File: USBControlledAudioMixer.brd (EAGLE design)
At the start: 42.5 x 40 mm, 50 parts, among them IC1 TDA7448, IC2 TS912, IC3 MEGA8-AI, J2 AVR_SPI_PRG_6NS, Q1 16MHz, U1 LMR62014

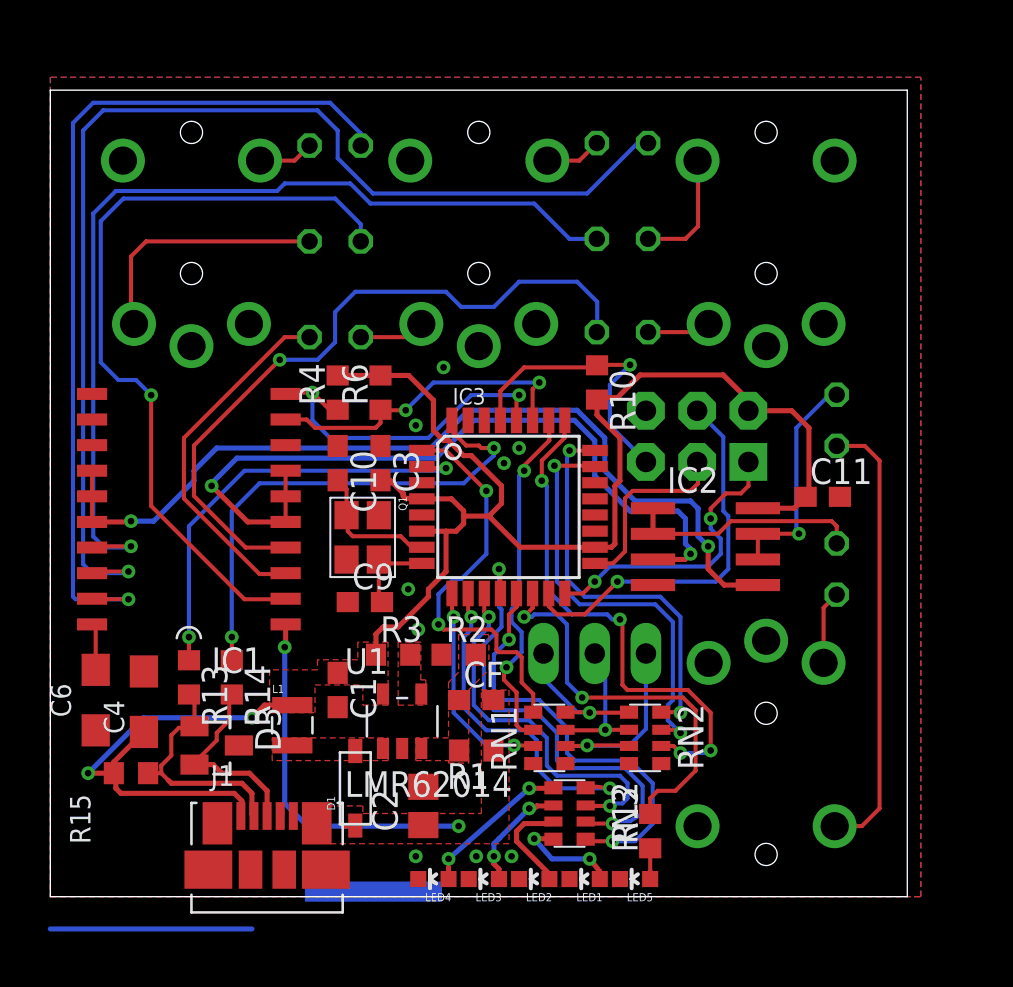
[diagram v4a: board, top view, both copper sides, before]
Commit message: Refactored whole board because due to case layout constraint, the regular through-hole film capacitors couldn't be used anymore. We're now using 1206 SMD film capacitors.
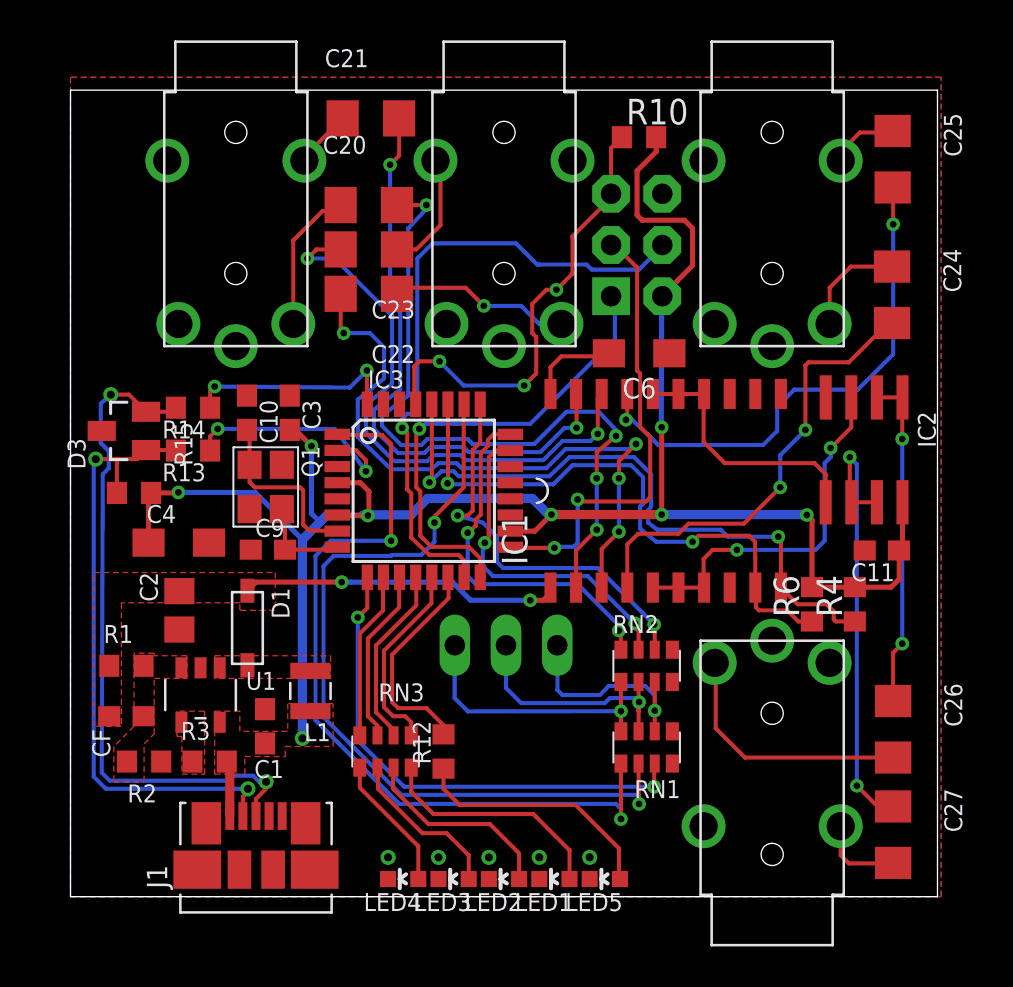
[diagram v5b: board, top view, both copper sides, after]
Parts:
- C20, C21, C22, C23, C24, C25, C26, C27: device rcl:C025-050X050 -> rcl:C1206
- JP2: device pinhead:1X03/90 -> TinyMix3:1X03/90_MOLEX_4094
- moved C6 32.0 mm to (29.2, 26.9), turned to 0 degrees
- moved R4 27.7 mm to (39.9, 14.5)
- moved R6 23.8 mm to (37.8, 14.5)
- moved IC1 23.7 mm to (30.5, 20.1), turned to 0 degrees
- moved C27 20.7 mm to (41.8, 3.08), flipped to the top
- moved R1 17.9 mm to (3.77, 11.4), turned to 0 degrees
- moved CF 17.4 mm to (3.77, 8.95), turned to 180 degrees
- moved R2 16.5 mm to (4.65, 6.70), turned to 180 degrees
- moved D3 16.3 mm to (3.65, 23.1), turned to 90 degrees
- moved C2 15.5 mm to (6.40, 14.2), turned to 270 degrees
- moved C25 14.0 mm to (41.8, 36.6), flipped to the top, turned to 270 degrees
- moved R15 13.9 mm to (4.15, 20.0), turned to 180 degrees
- moved C23 13.6 mm to (15.8, 32.1), flipped to the top
- moved R14 13.5 mm to (7.08, 24.2), turned to 180 degrees
- moved C24 13.5 mm to (41.8, 29.9), flipped to the top, turned to 270 degrees
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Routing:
- net OUT_R: track 44.2 -> 13.0 mm, vias 2 -> 0
- net IN_2_R: track 57.8 -> 28.5 mm, vias 1 -> 2
- net N$13: track 9.63 -> 33.4 mm, vias 0 -> 2
- net TOUCH_SEND_+: track 17.7 -> 40.9 mm
- net IN_3_R: track 46.8 -> 25.9 mm, vias 1 -> 2
- net OUT_L: track 38.7 -> 18.0 mm
- net TOUCH_SEND_-: track 20.1 -> 40.1 mm
- net N$11: track 11.8 -> 31.0 mm, vias 0 -> 2
- net N$26: track 22.3 -> 4.22 mm
- net SCL: track 17.2 -> 32.3 mm
- net IN_1_R: track 44.0 -> 29.4 mm, vias 1 -> 2
- net TOUCH_SEND_CHAN: track 10.6 -> 25.1 mm
- net IN_2_L: track 17.9 -> 32.4 mm, vias 0 -> 4
- net D+: track 24.8 -> 10.7 mm
- net LED2: track 23.0 -> 9.04 mm, vias 2 -> 0
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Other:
- board size 42.5 x 40 mm -> 43 x 40 mm

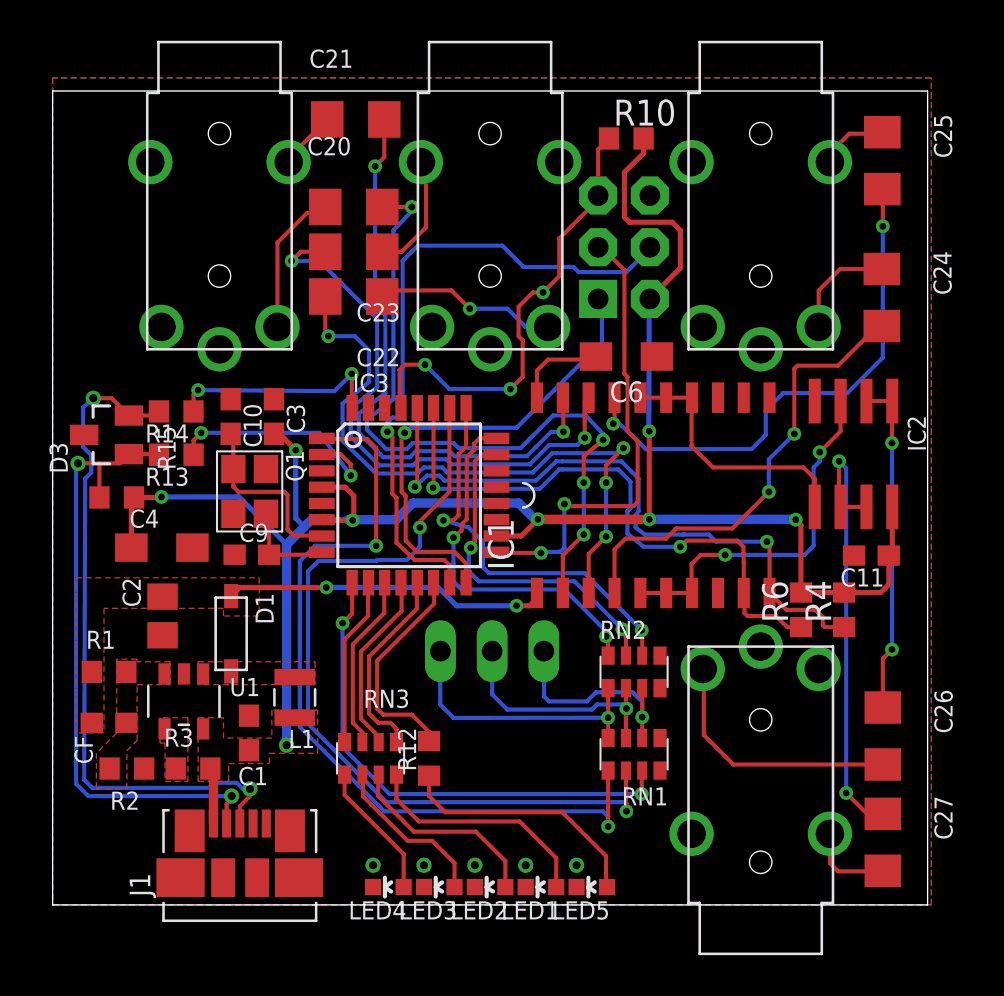
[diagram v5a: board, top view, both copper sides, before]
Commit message: Semi-finalized board, front and back panel Added 100nF capacitor for the TDA7448 mixer
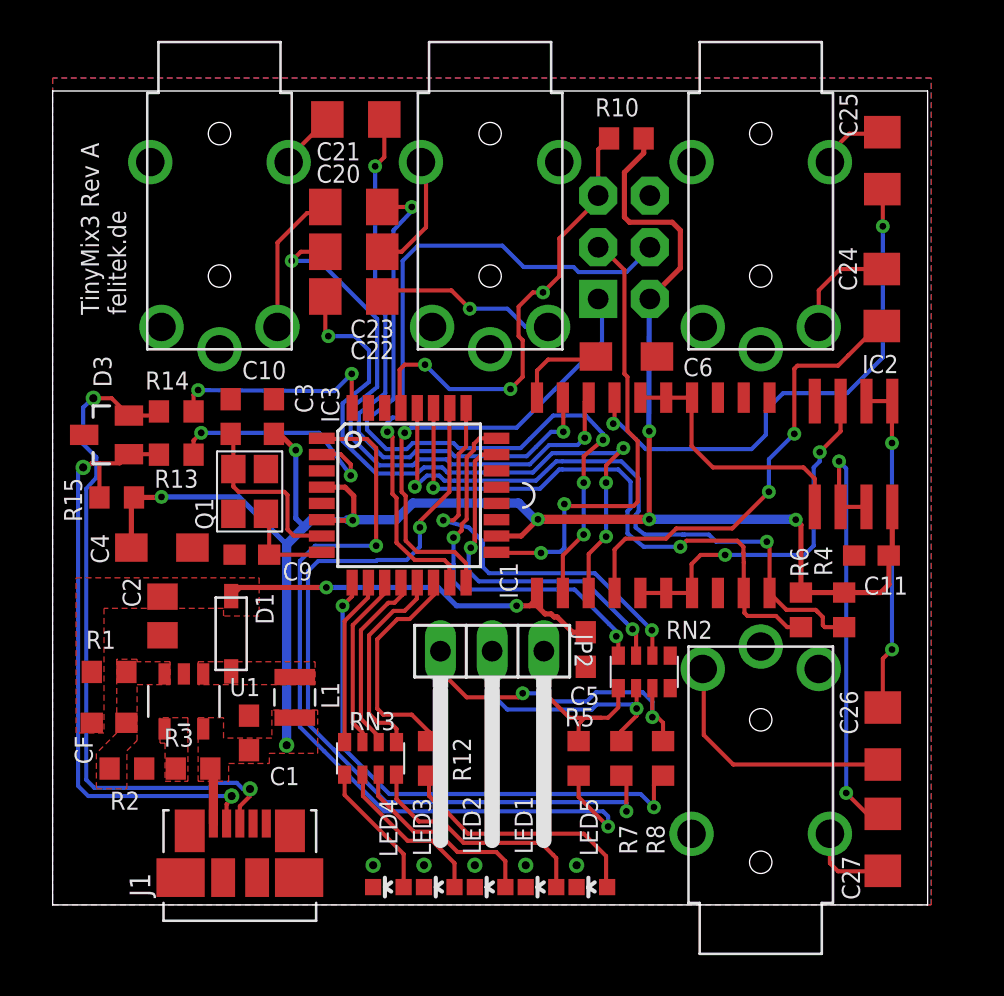
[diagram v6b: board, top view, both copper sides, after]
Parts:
- removed RN1: 1M, Simplex-rlc:YC164
- added C5: 100n, rcl:C0603
- added R5, R7, R8: 22M, rcl:R0603
- moved RN2 0.50 mm to (30.1, 11.4)
- flipped JP2 to the top
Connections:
- net +9V: now also C5.1
- net GND: now also C5.2
- net N$18: now also R5.2; no longer RN1.4
- net N$19: now also R7.2; no longer RN1.3
- net N$20: now also R8.2; no longer RN1.2
- net TOUCH_SEND_+: now also R7.1; no longer RN1.6
- net TOUCH_SEND_-: now also R5.1; no longer RN1.5
- net TOUCH_SEND_CHAN: now also R8.1; no longer RN1.7
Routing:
- net N$20: track 10.7 -> 16.3 mm, vias 1 -> 2
- net N$18: track 13.6 -> 9.43 mm, vias 1 -> 0
- net +9V: track 16.0 -> 19.2 mm
- net TOUCH_SEND_CHAN: track 25.1 -> 26.5 mm
- net TOUCH_RCV_+: track 17.4 -> 18.0 mm
- net TOUCH_RCV_CHAN: track 20.2 -> 20.7 mm
- net TOUCH_RCV_-: track 18.2 -> 18.7 mm
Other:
- board text added: "TinyMix3 Rev A felitek.de"

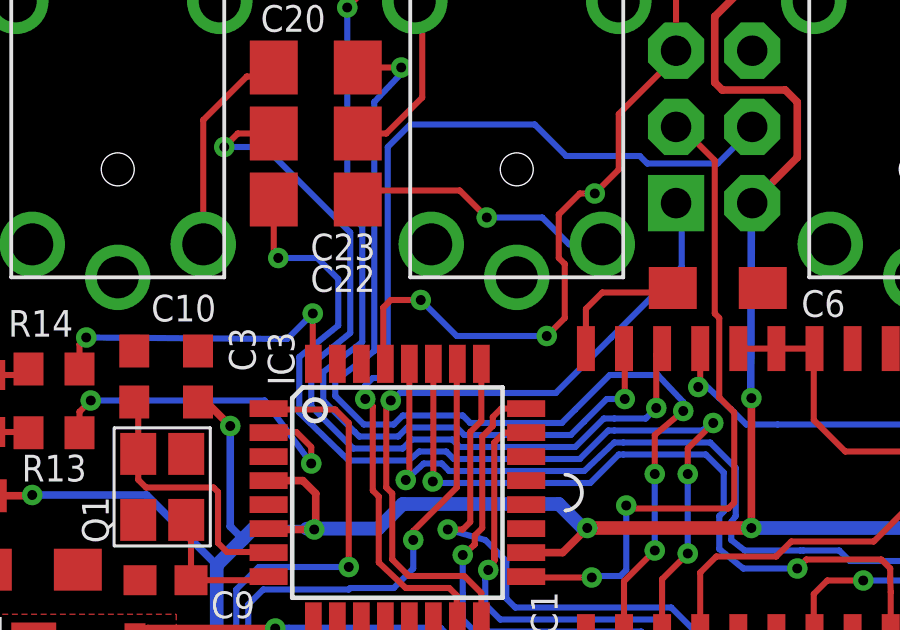
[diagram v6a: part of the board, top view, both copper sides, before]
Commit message: Added ESD protection for the RESET line
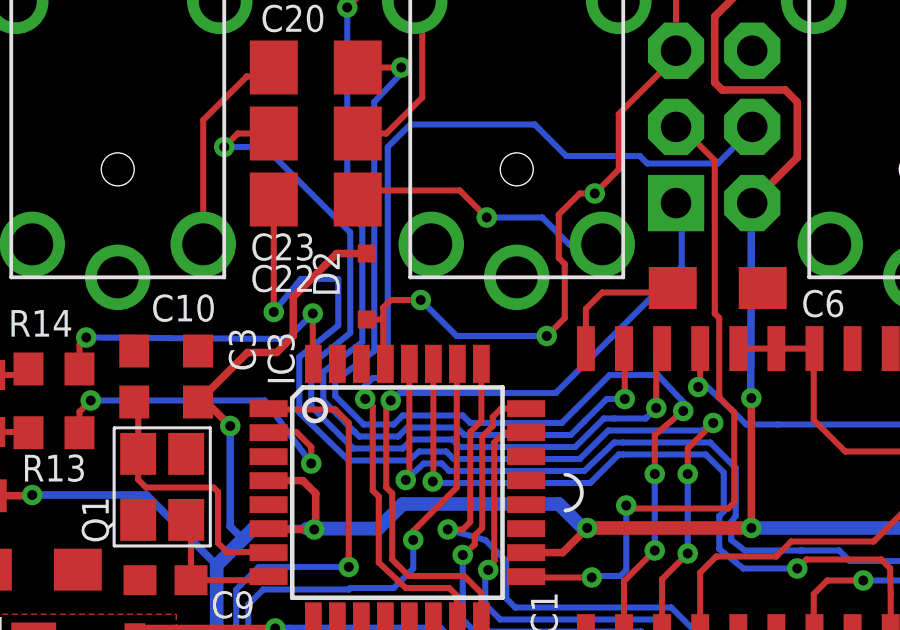
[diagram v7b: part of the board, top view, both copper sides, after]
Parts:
- added D2: (no value), diode:SOD323-R
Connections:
- net +5V: now also D2.C
- net RESET: now also D2.A
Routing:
- net +5V: track 96.5 -> 104.9 mm
- net IN_2_L: track 32.4 -> 34.5 mm
- net RESET: track 22.9 -> 23.5 mm
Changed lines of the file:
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@@
 <?xml version="1.0" encoding="utf-8"?>
 <!DOCTYPE eagle SYSTEM "eagle.dtd">
-<eagle version="6.6.0">
+<eagle version="6.5.0">
 <drawing>
 <settings>
@@
 <setting verticaltext="up"/>
 </settings>
-<grid distance="0.500000001" unitdist="mm" unit="mm" style="lines" multiple="1" display="no" altdistance="0.05" altunitdist="mm" altunit="mm"/>
+<grid distance="19.6850394" unitdist="mil" unit="mil" style="lines" multiple="1" display="no" altdistance="0.05" altunitdist="mm" altunit="mm"/>
 <layers>
 <layer number="1" name="Top" color="4" fill="1" visible="yes" active="yes"/>
@@
 <attribute name="NAME" x="12.307" y="15.945" size="0.889" layer="25"/>
 <attribute name="OC_DIGIKEY" value="1276-1254-1-ND" x="10.792" y="17.21" size="1.778" layer="27" display="off"/>
-<attribute name="PRICE_100" value="0.126" x="10.792" y="17.21" size="1.778" layer="27" display="off"/>
+<attribute name="PRICE_100" value="0.013" x="10.792" y="17.21" size="1.778" layer="27" display="off"/>
 </element>
 <element name="R10" library="rcl" package="R0603" value="10k" x="29.195" y="37.665" smashed="yes">
@@
 <element name="C22" library="rcl" package="C1206" value="470n" x="15.8" y="29.9" smashed="yes" rot="R180">
 <attribute name="PRICE_100" value="0.487" x="15.8" y="29.9" size="1.778" layer="27" rot="R180" display="off"/>
-<attribute name="NAME" x="17.786" y="27.71" size="0.889" layer="25" ratio="10" rot="R180"/>
+<attribute name="NAME" x="15.786" y="27.71" size="0.889" layer="25" ratio="10" rot="R180"/>
 <attribute name="OC_DIGIKEY" value="338-2776-1-ND" x="15.8" y="29.9" size="1.778" layer="27" rot="R180" display="off"/>
 </element>
 <element name="C23" library="rcl" package="C1206" value="470n" x="15.8" y="32.1" smashed="yes" rot="R180">
 <attribute name="PRICE_100" value="0.487" x="15.8" y="32.1" size="1.778" layer="27" rot="R180" display="off"/>
-<attribute name="NAME" x="17.786" y="28.76" size="0.889" layer="25" ratio="10" rot="R180"/>
+<attribute name="NAME" x="15.786" y="28.76" size="0.889" layer="25" ratio="10" rot="R180"/>
 <attribute name="OC_DIGIKEY" value="338-2776-1-ND" x="15.8" y="32.1" size="1.778" layer="27" rot="R180" display="off"/>
 </element>
@@
 <attribute name="OC_DIGIKEY" value="1276-1258-1-ND" x="27.2" y="12.55" size="1.778" layer="27" rot="R270" display="off"/>
 <attribute name="NAME" x="26.415" y="9.835" size="0.889" layer="25"/>
+</element>
+<element name="D2" library="diode" package="SOD323-R" value="" x="17.5" y="27" smashed="yes" rot="R270">
+<attribute name="OC_DIGIKEY" value="497-10893-1-ND" x="17.5" y="27" size="1.778" layer="27" rot="R270" display="off"/>
+<attribute name="PRICE_100" value="0.092" x="17.5" y="27" size="1.778" layer="27" rot="R270" display="off"/>
+<attribute name="NAME" x="16.6" y="26.65" size="0.889" layer="25" rot="R90"/>
+<attribute name="VALUE" x="15.2" y="28.1" size="1.27" layer="27" rot="R270"/>
 </element>
 </elements>
@@
 <wire x1="15.75" y1="18.9" x2="15.53" y2="18.9" width="0.254" layer="16"/>
 <wire x1="15.53" y1="18.9" x2="15.5" y2="18.93" width="0.254" layer="16"/>
+<contactref element="D2" pad="C"/>
+<wire x1="17.5" y1="28.1" x2="16.5" y2="28.1" width="0.254" layer="1"/>
+<wire x1="16.5" y1="28.1" x2="15.05" y2="26.65" width="0.254" layer="1"/>
+<wire x1="15.05" y1="26.65" x2="15.05" y2="25.35" width="0.254" layer="1"/>
+<wire x1="15.05" y1="25.35" x2="14.5" y2="24.8" width="0.254" layer="1"/>
+<wire x1="14.5" y1="24.8" x2="13.525" y2="24.8" width="0.254" layer="1"/>
+<wire x1="13.525" y1="24.8" x2="11.875" y2="23.15" width="0.254" layer="1"/>
 </signal>
 <signal name="MISO">
@@
 <wire x1="19.3" y1="26.55" x2="18.3" y2="26.55" width="0.2032" layer="1"/>
 <wire x1="18.3" y1="26.55" x2="18.05" y2="26.3" width="0.2032" layer="1"/>
-<wire x1="18.05" y1="26.3" x2="18.05" y2="24.4926" width="0.2032" layer="1"/>
+<wire x1="18.05" y1="26.3" x2="18.05" y2="26" width="0.2032" layer="1"/>
+<wire x1="18.05" y1="25.9" x2="18.05" y2="24.4926" width="0.2032" layer="1"/>
 <wire x1="18.05" y1="24.4926" x2="18.12" y2="24.4226" width="0.2032" layer="1"/>
 <via x="23.5" y="25.35" extent="1-16" drill="0.3302"/>
 <via x="19.3" y="26.55" extent="1-16" drill="0.3302"/>
+<contactref element="D2" pad="A"/>
+<wire x1="17.5" y1="25.9" x2="18.05" y2="25.9" width="0.2032" layer="1"/>
+<wire x1="18.05" y1="25.9" x2="18.05" y2="26" width="0.2032" layer="1"/>
 </signal>
 <signal name="MOSI">
@@
 <contactref element="IC1" pad="3"/>
 <contactref element="C22" pad="2"/>
-<wire x1="14.4" y1="29.9" x2="14.4" y2="28.1" width="0.2032" layer="1"/>
-<wire x1="14.4" y1="28.1" x2="14.55" y2="27.95" width="0.2032" layer="1"/>
-<via x="14.55" y="27.95" extent="1-16" drill="0.3302"/>
-<wire x1="14.55" y1="27.95" x2="15.85" y2="27.95" width="0.2032" layer="16"/>
-<wire x1="15.85" y1="27.95" x2="16.55" y2="27.25" width="0.2032" layer="16"/>
+<wire x1="14.4" y1="29.9" x2="14.4" y2="26.15" width="0.2032" layer="1"/>
+<via x="14.4" y="26.15" extent="1-16" drill="0.3302"/>
+<wire x1="14.4" y1="26.15" x2="15.3" y2="27.25" width="0.2032" layer="16"/>
+<wire x1="15.3" y1="27.25" x2="16.55" y2="27.25" width="0.2032" layer="16"/>
 <wire x1="16.55" y1="27.25" x2="16.55" y2="25.7" width="0.2032" layer="16"/>
 <wire x1="27.345" y1="15.33" x2="27.345" y2="17.245" width="0.2032" layer="1"/>
@@
 <wire x1="29.05" y1="22.45" x2="28.95" y2="22.45" width="0.2032" layer="16"/>
 <wire x1="28.95" y1="22.45" x2="28.7" y2="22.2" width="0.2032" layer="16"/>
-<wire x1="28.7" y1="22.2" x2="25.75" y2="22.2" width="0.2032" layer="16"/>
-<wire x1="25.75" y1="22.2" x2="25.55" y2="22.2" width="0.2032" layer="16"/>
+<wire x1="28.7" y1="22.2" x2="25.55" y2="22.2" width="0.2032" layer="16"/>
 <wire x1="25.55" y1="22.2" x2="24.6" y2="21.25" width="0.2032" layer="16"/>
 <wire x1="24.6" y1="21.25" x2="20.4" y2="21.25" width="0.2032" layer="16"/>
